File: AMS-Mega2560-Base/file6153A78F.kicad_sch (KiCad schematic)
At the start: 21 parts, among them IC7 LTV-846S, Q1 2N7000, Q2 2N7000, Q3 2N7000, Q4 2N7000

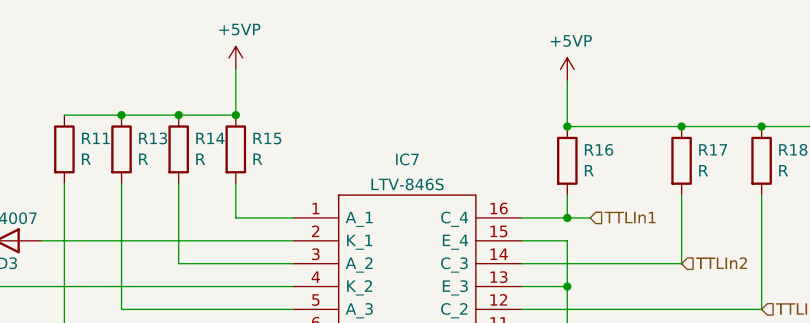
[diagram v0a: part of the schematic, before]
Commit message: fixing the 5V lines and removing the 5V fromt he MCU board and only using the 3Amp 5v power supplied by CampKeen
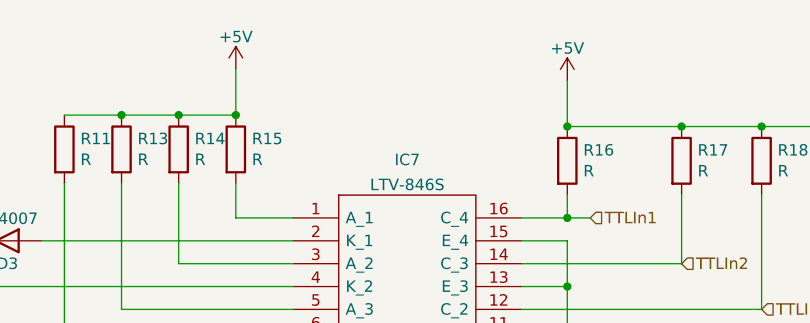
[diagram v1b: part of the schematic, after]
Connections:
- net +5VP renamed +5V
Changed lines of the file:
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@@
     (pin "1")
   )
-  (symbol (lib_id "power:+5VP") (at 190.5 27.94 0) (unit 1)
-    (in_bom yes) (on_board yes)
-    (property "Reference" "#PWR045" (id 0) (at 190.5 31.75 0)
-      (effects (font (size 1.27 1.27)) hide)
-    )
-    (property "Value" "+5VP" (id 1) (at 190.881 23.5458 0))
+  (symbol (lib_id "power:+5V") (at 190.5 27.94 0) (unit 1)
+    (in_bom yes) (on_board yes) (fields_autoplaced)
+    (property "Reference" "#PWR?" (id 0) (at 190.5 31.75 0)
+      (effects (font (size 1.27 1.27)) hide)
+    )
+    (property "Value" "+5V" (id 1) (at 190.5 24.3355 0))
     (property "Footprint" "" (id 2) (at 190.5 27.94 0)
       (effects (font (size 1.27 1.27)) hide)
@@
     (pin "1")
     (pin "2")
+  )
+  (symbol (lib_id "power:+5V") (at 227.33 29.21 0) (unit 1)
+    (in_bom yes) (on_board yes) (fields_autoplaced)
+    (property "Reference" "#PWR?" (id 0) (at 227.33 33.02 0)
+      (effects (font (size 1.27 1.27)) hide)
+    )
+    (property "Value" "+5V" (id 1) (at 227.33 25.6055 0))
+    (property "Footprint" "" (id 2) (at 227.33 29.21 0)
+      (effects (font (size 1.27 1.27)) hide)
+    )
+    (property "Datasheet" "" (id 3) (at 227.33 29.21 0)
+      (effects (font (size 1.27 1.27)) hide)
+    )
+    (pin "1")
   )
   (symbol (lib_id "power:GND") (at 168.91 121.92 0) (unit 1)
@@
     (pin "2")
   )
-  (symbol (lib_id "power:+5VP") (at 227.33 29.21 0) (unit 1)
-    (in_bom yes) (on_board yes)
-    (property "Reference" "#PWR046" (id 0) (at 227.33 33.02 0)
-      (effects (font (size 1.27 1.27)) hide)
-    )
-    (property "Value" "+5VP" (id 1) (at 227.711 24.8158 0))
-    (property "Footprint" "" (id 2) (at 227.33 29.21 0)
-      (effects (font (size 1.27 1.27)) hide)
-    )
-    (property "Datasheet" "" (id 3) (at 227.33 29.21 0)
-      (effects (font (size 1.27 1.27)) hide)
-    )
-    (pin "1")
-  )
   (symbol (lib_id "Transistor_FET:2N7000") (at 166.37 104.14 0) (unit 1)
